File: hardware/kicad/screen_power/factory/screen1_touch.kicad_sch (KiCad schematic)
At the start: 12 parts, among them J101 PI USB, J102 TOUCH, U101 ADuM3165BRSZ, Y101 24MHz 10pF

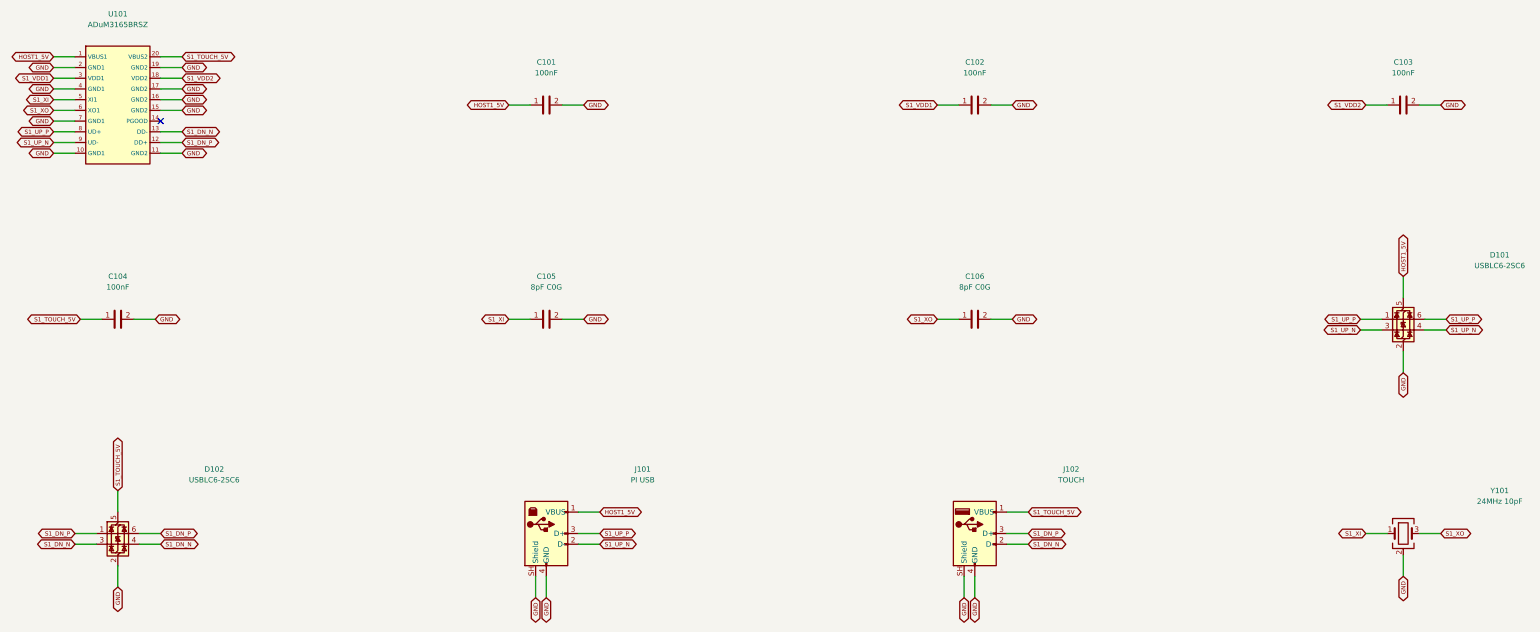
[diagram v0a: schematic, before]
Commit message: refactor(hardware): simplify and compact screen power boards
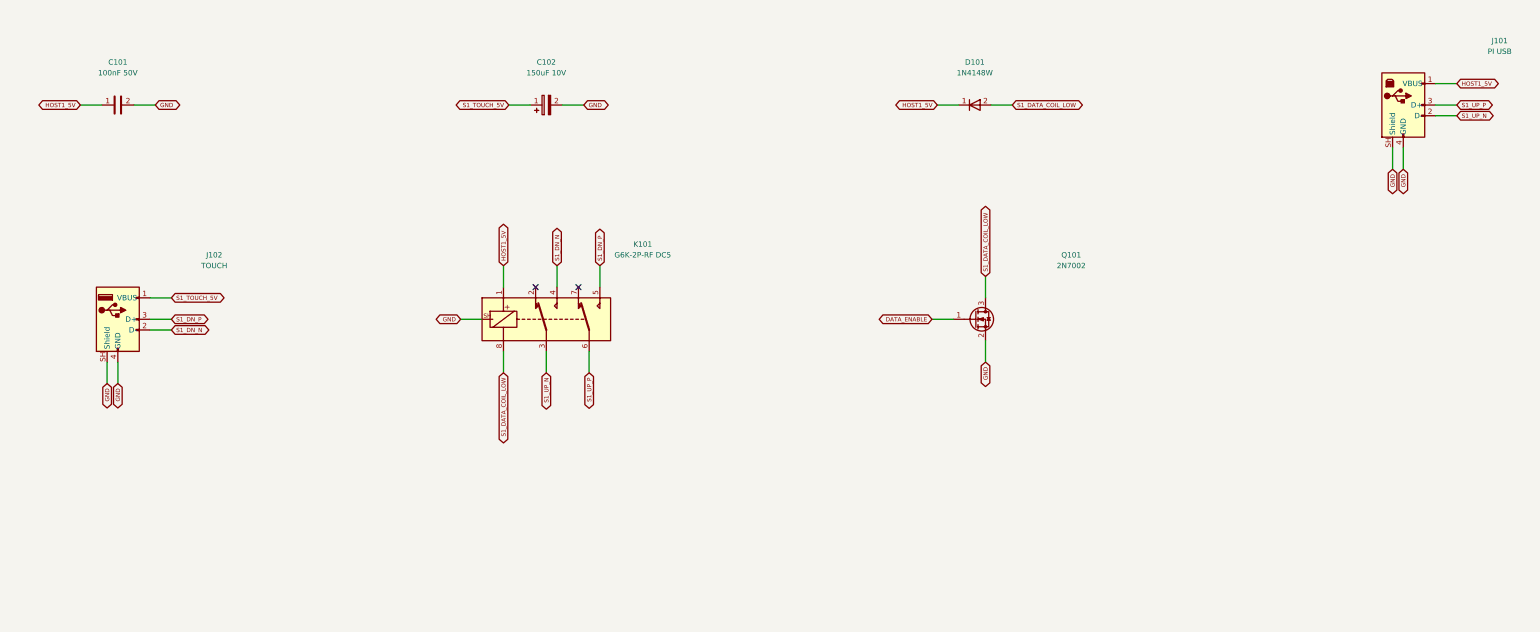
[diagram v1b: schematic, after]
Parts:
- removed C103, C104: 100nF, Capacitor_SMD:C_0805_2012Metric, symbol screen_symbols:Device_C
- removed C105, C106: 8pF C0G, Capacitor_SMD:C_0805_2012Metric, symbol screen_symbols:Device_C
- removed D102: USBLC6-2SC6, Package_TO_SOT_SMD:SOT-23-6, symbol screen_symbols:Power_Protection_USBLC6-2SC6
- removed U101: ADuM3165BRSZ, Package_SO:SSOP-20_5.3x7.2mm_P0.65mm, symbol screen_symbols:screen_power_ADuM3165BRSZ
- removed Y101: 24MHz 10pF, Crystal:Crystal_SMD_3225-4Pin_3.2x2.5mm, symbol screen_symbols:Device_Crystal_GND24
- added K101: G6K-2P-RF DC5, screen_power:Relay_DPDT_Omron_G6K-2P-RF, symbol screen_symbols:screen_power_G6K-2P-RF
- added Q101: 2N7002, Package_TO_SOT_SMD:SOT-23, symbol screen_symbols:Transistor_FET_2N7002
- C101: value 100nF -> 100nF 50V; MPN C0805C104K5RAC -> GRM21BR71H104KA01L
- C102: value 100nF -> 150uF 10V; footprint Capacitor_SMD:C_0805_2012Metric -> Capacitor_THT:CP_Radial_D5.0mm_P2.00mm; symbol screen_symbols:Device_C -> screen_symbols:Device_C_Polarized; MPN C0805C104K5RAC -> EEU-FR1A151
- D101: value USBLC6-2SC6 -> 1N4148W; footprint Package_TO_SOT_SMD:SOT-23-6 -> Diode_SMD:D_SOD-123; symbol screen_symbols:Power_Protection_USBLC6-2SC6 -> screen_symbols:Diode_1N4148W; MPN USBLC6-2SC6 -> 1N4148W-7-F
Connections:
- net S1_VDD1 is gone; now on net S1_TOUCH_5V: C102.1
- net GND: now also K101.SH (CASE), Q101.2 (S); no longer D101.2 (GND)
- net HOST1_5V: now also D101.1 (K), K101.1; no longer D101.5 (VBUS)
- net S1_DN_N: now also K101.4
- net S1_DN_P: now also K101.5
- net S1_UP_N: now also K101.3; no longer D101.3 (I/O2), D101.4 (I/O2)
- net S1_UP_P: now also K101.6; no longer D101.1 (I/O1), D101.6 (I/O1)
- new net DATA_ENABLE: Q101.1 (G)
- new net S1_DATA_COIL_LOW: D101.2 (A), K101.8, Q101.3 (D)
- no-connect marks 1 -> 2
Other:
- moved on the sheet: C101, J101, J102
